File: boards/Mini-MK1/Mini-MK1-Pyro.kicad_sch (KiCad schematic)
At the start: 29 parts, among them U1 TCAL9538-UQFN, U2 PTPS3842A011DRLRQ1, U3 MAX14575CETA+

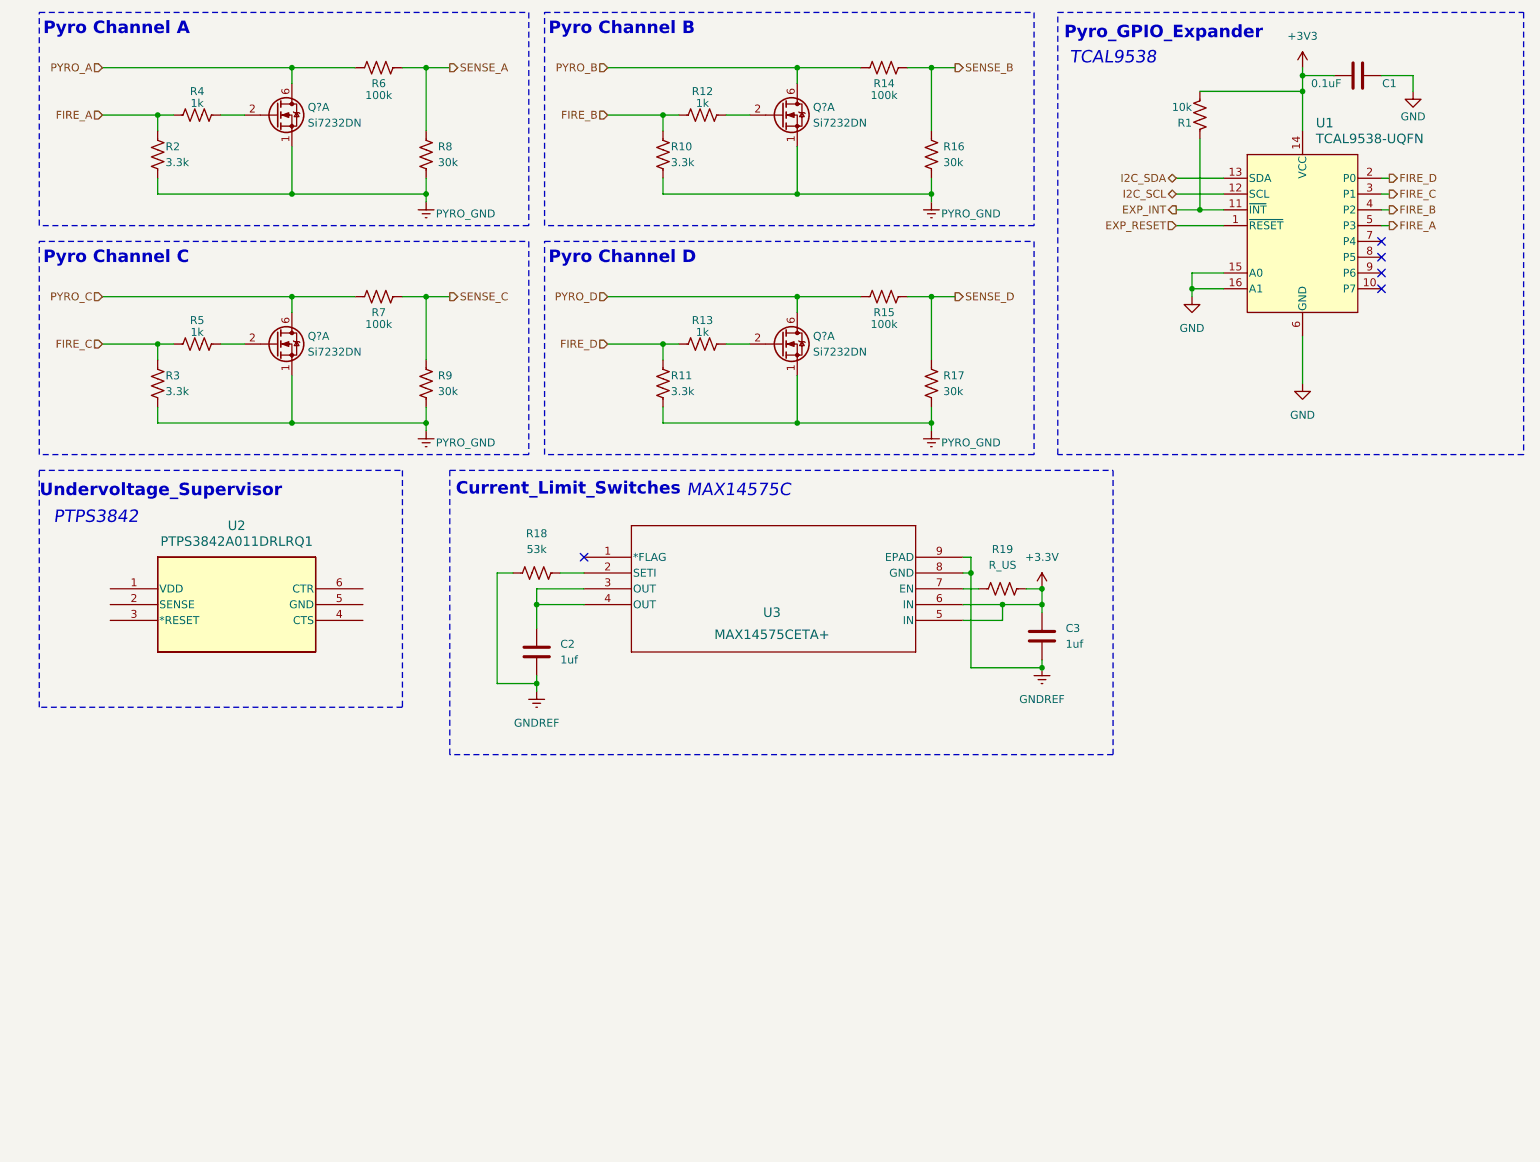
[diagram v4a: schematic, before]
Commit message: Added Undervoltage Supervisor, fix bugs
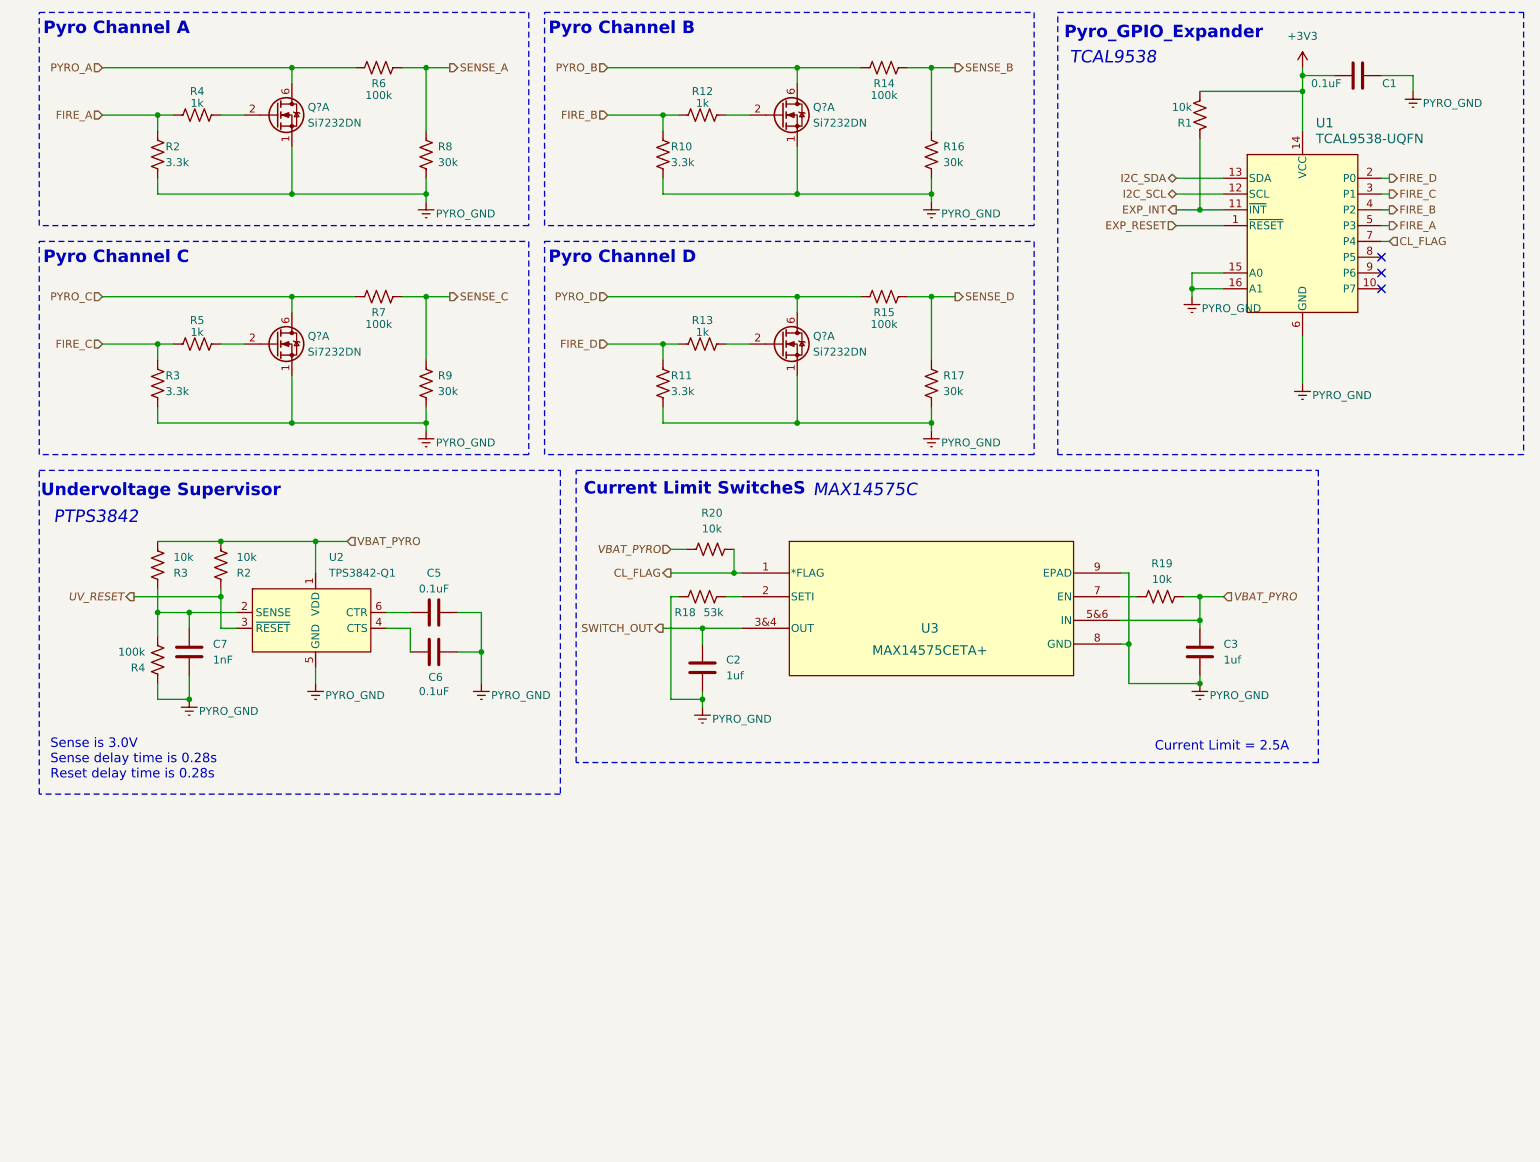
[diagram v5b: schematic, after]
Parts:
- removed U2: PTPS3842A011DRLRQ1, SOT-5X3-6_DRL_TEX, symbol Power_Supervisor:PTPS3842A011DRLRQ1
- added 100k: R4, symbol Device:R_US
- added 10k: R2, symbol Device:R_US
- added 10k: R3, symbol Device:R_US
- added C5, C6: 0.1uF, symbol Device:C
- added C7: 1nF, symbol Device:C
- added R20: 10k, symbol Device:R_US
- added U2: TPS3842-Q1, Package_TO_SOT_SMD:Texas_R-PDSO-N6_DRL-6, symbol Power_Supervisor_Texas:TPS3842-Q1
- R19: value R_US -> 10k
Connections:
- net GND is gone; now on net PYRO_GND: C1.1, U1.15 (A0), U1.16 (A1), U1.6 (GND)
- net GNDREF is gone; now on net PYRO_GND: C2.2, C3.2, R18.1, U3.8 (GND), U3.9 (EPAD)
- net PYRO_GND: now also 100k.2, C5.2, C6.2, C7.1, U2.5 (GND)
- net CL_FLAG: now reaches U3.1 (*FLAG)
- net CL_FLAG: now also U1.7 (P4), R20.2
- net +3.3V renamed VBAT_PYRO
- net VBAT_PYRO: now also U3. (IN), U3.5&6 (IN), 10k.1, 10k.1, R20.1, U2.1 (VDD); no longer U3.5 (IN), U3.6 (IN)
- new net: 100k.1, 10k.2, C7.2, U2.2 (SENSE)
- new net: C6.1, U2.4 (CTS)
- new net: C5.1, U2.6 (CTR)
- new net SWITCH_OUT: C2.1, U3. (IN), U3.3&4 (OUT)
- new net UV_RESET: 10k.2, U2.3 (~{RESET})
- no-connect marks 5 -> 3
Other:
- note added: "Current Limit = 2.5A"
- note added: "Current Limit SwitcheS"
- note added: "Sense is 3.0V Sense delay time is 0.28s Reset delay time is 0.28s"
- note added: "Undervoltage Supervisor"
- note removed: "Current_Limit_Switches"
- note removed: "Undervoltage_Supervisor"
- moved on the sheet: C2, C3, R18, R19

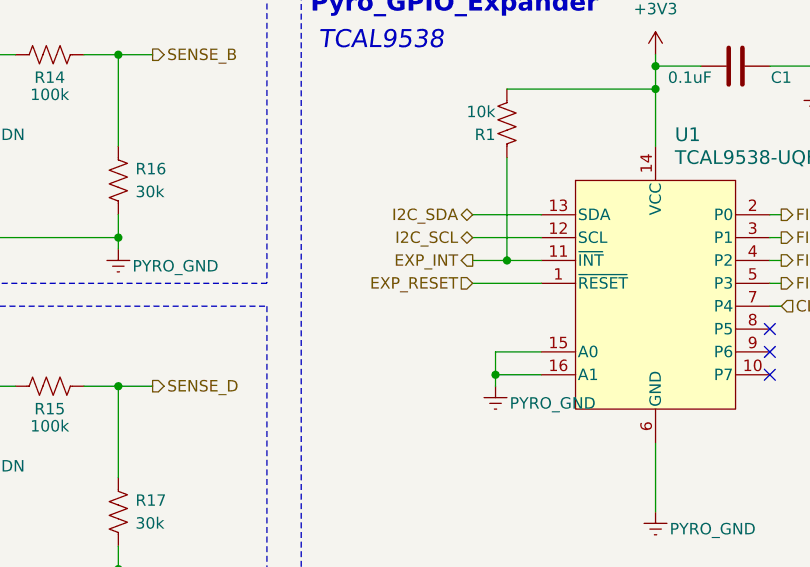
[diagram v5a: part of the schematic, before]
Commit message: Changed to UV_Reset
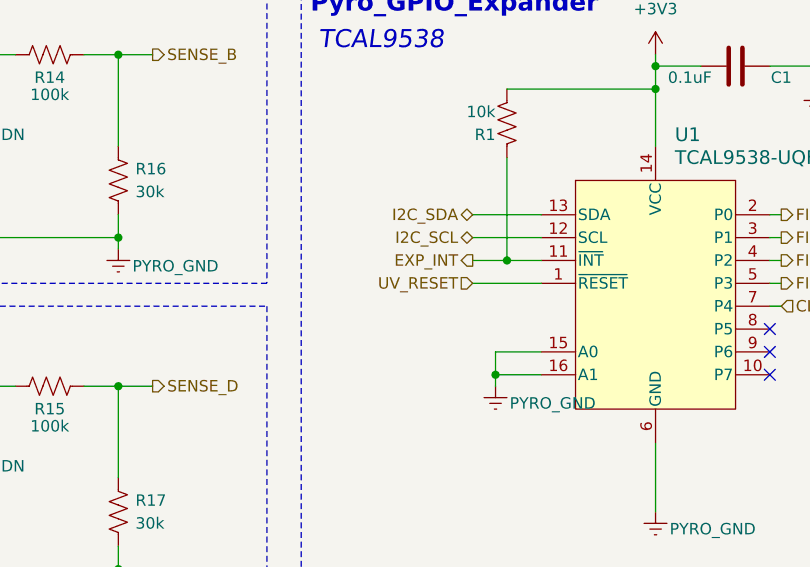
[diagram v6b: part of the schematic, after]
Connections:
- net EXP_RESET is gone; now on net UV_RESET: U1.1 (~{RESET})
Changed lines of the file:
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@@
 		)
 	)
-	(hierarchical_label "EXP_RESET"
+	(hierarchical_label "UV_RESET"
 		(shape input)
 		(at 198.12 48.26 180)

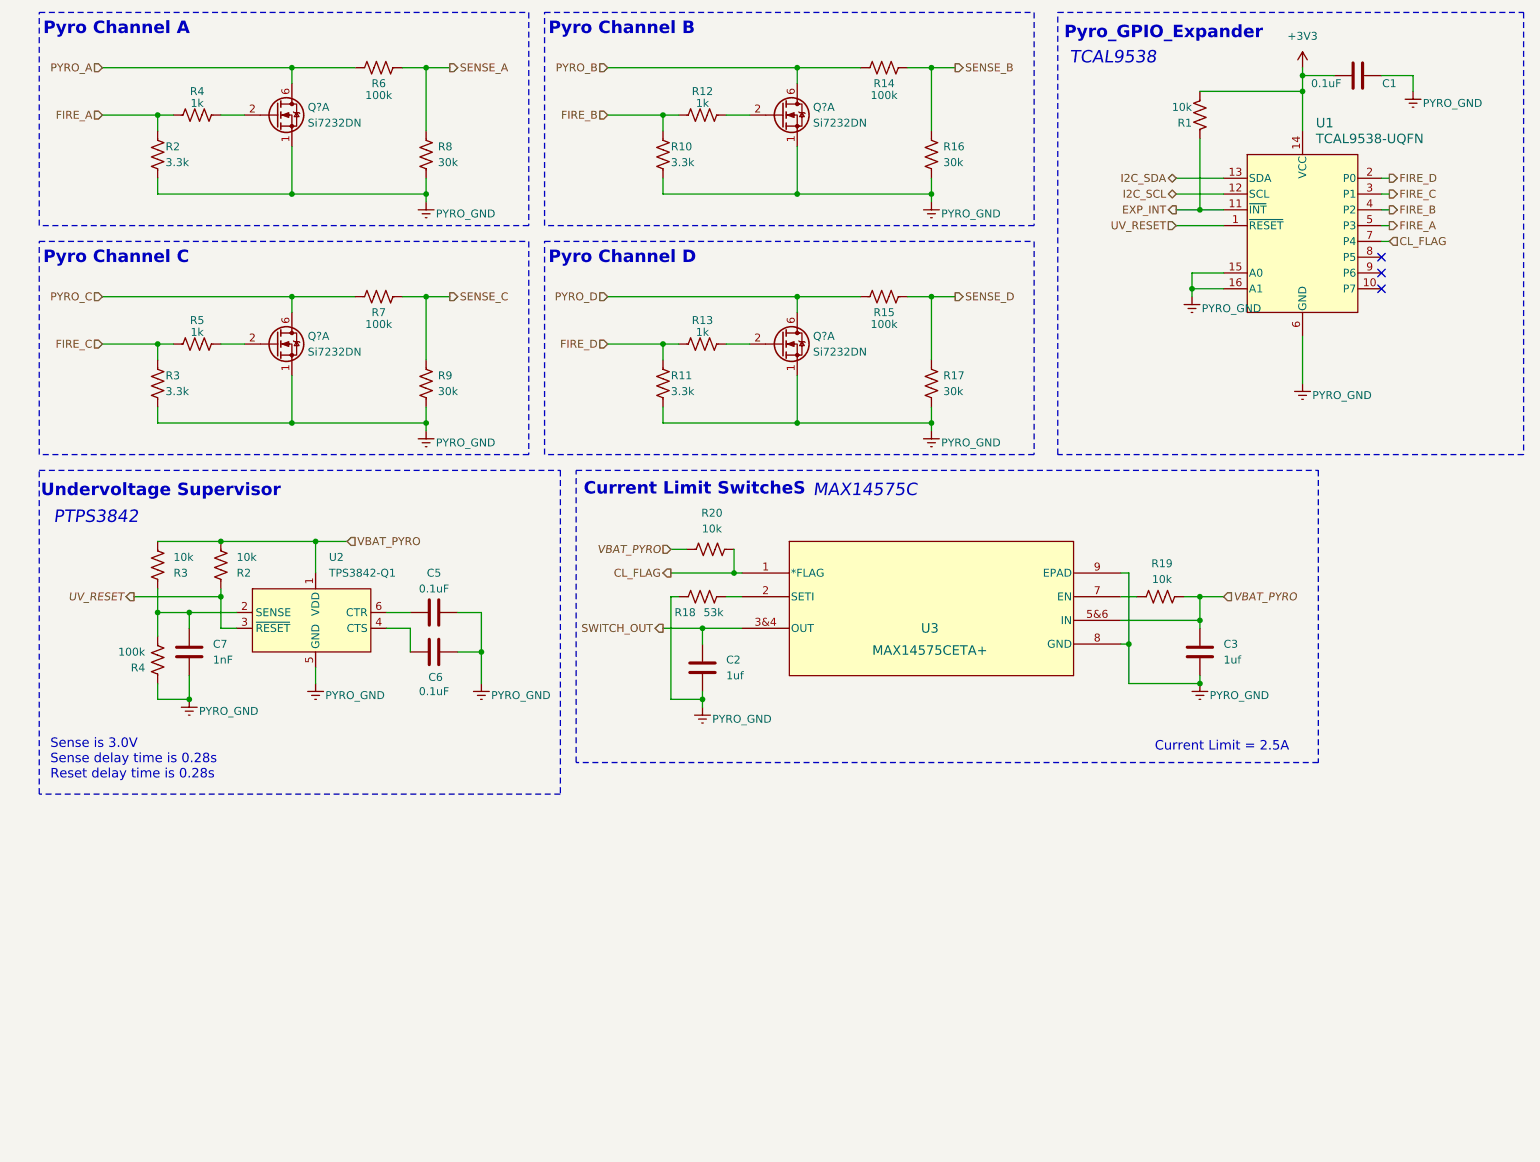
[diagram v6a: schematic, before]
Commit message: Change some of the outputs and inputs, replace pyro ground, check 12c address
Undervoltage supervisor needs to be cut but I didn't have the heart to do it. Changed baro spi's to the correct ones. Enable of the MAX is from pyro global enable.
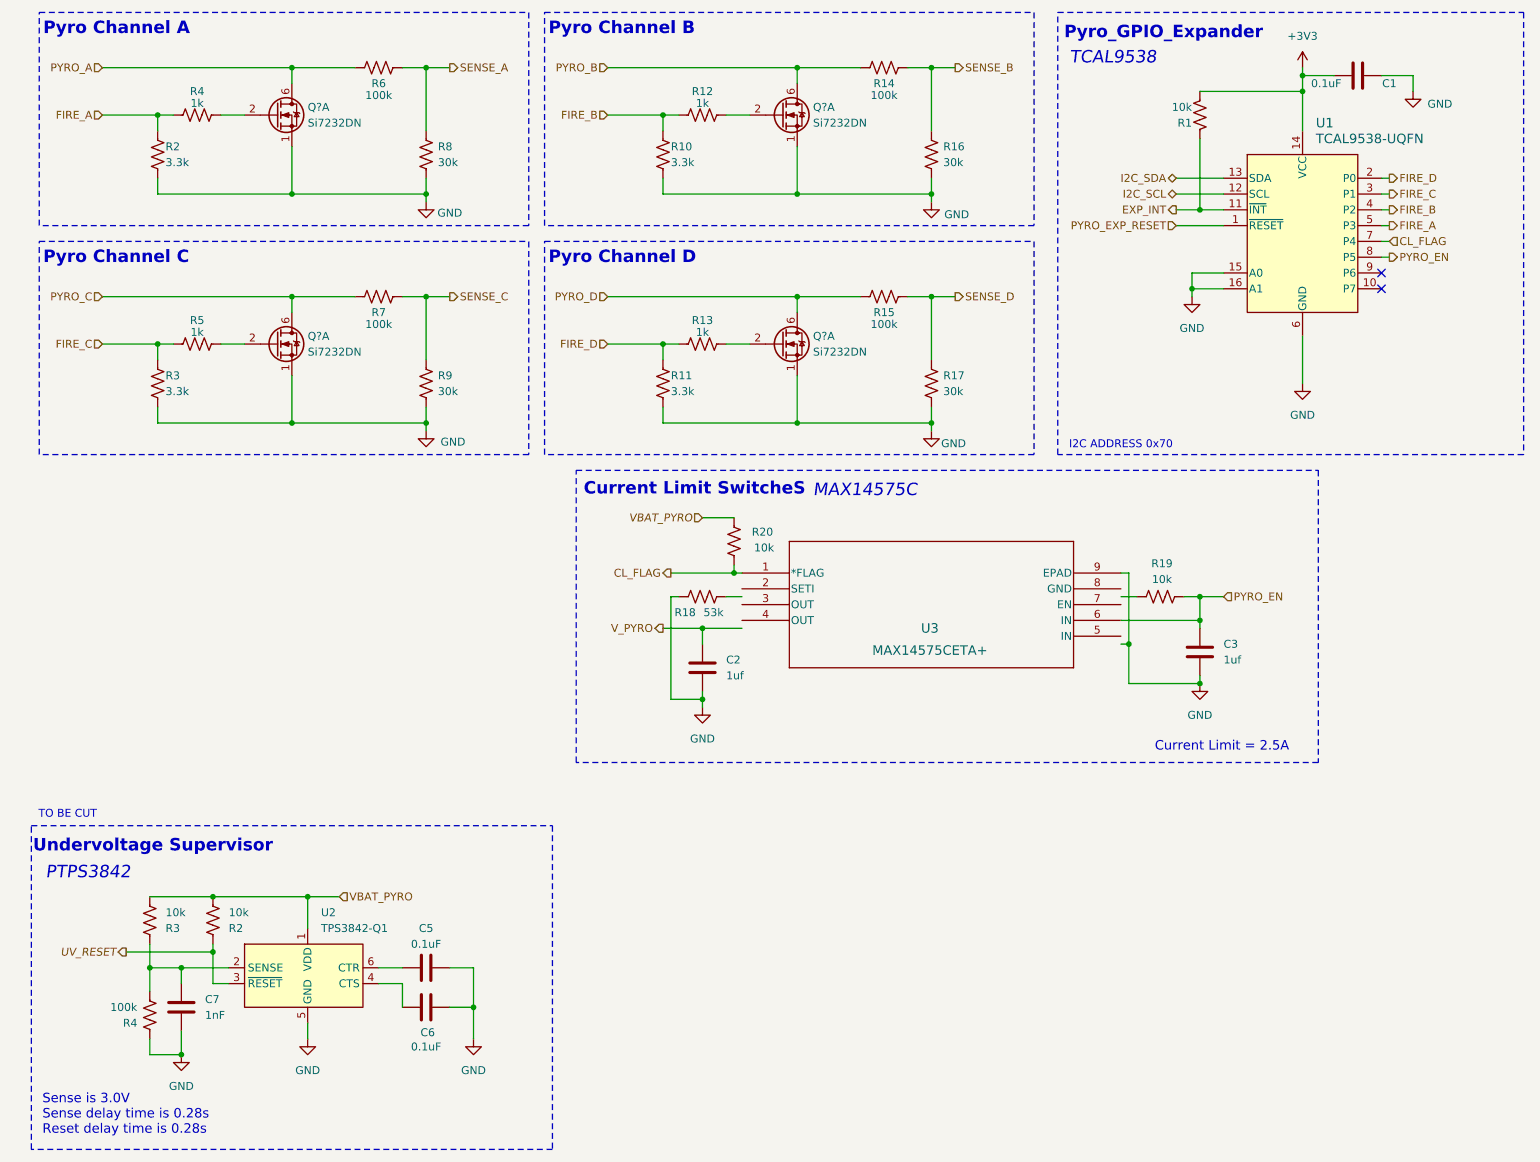
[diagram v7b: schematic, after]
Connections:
- net UV_RESET: no longer U1.1 (~{RESET})
- net VBAT_PYRO: no longer C3.1, R19.2, U3. (IN), U3.5&6 (IN)
- net at R18.2: no longer U3.2 (SETI)
- net at U3.7 (EN): no longer R19.1
- net PYRO_EN: now reaches U1.8 (P5)
- net PYRO_EN: now also C3.1, R19.2, U3.6 (IN)
- net PYRO_GND renamed GND
- net GND: no longer U3.8 (GND)
- removed net SWITCH_OUT: C2.1, U3. (IN), U3.3&4 (OUT)
- new net PYRO_EXP_RESET: U1.1 (~{RESET})
- new net V_PYRO: C2.1
- no-connect marks 3 -> 2
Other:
- note added: "I2C ADDRESS 0x70"
- note added: "TO BE CUT"
- moved on the sheet: 100k, 10k, C5, C6, C7, R20, U2
